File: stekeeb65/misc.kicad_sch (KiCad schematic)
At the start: 7 parts, among them J1 TYPE-C-31-M12_13_EDITED, J2 Conn_02x03_Odd_Even, U1 WE-TVS-82400102

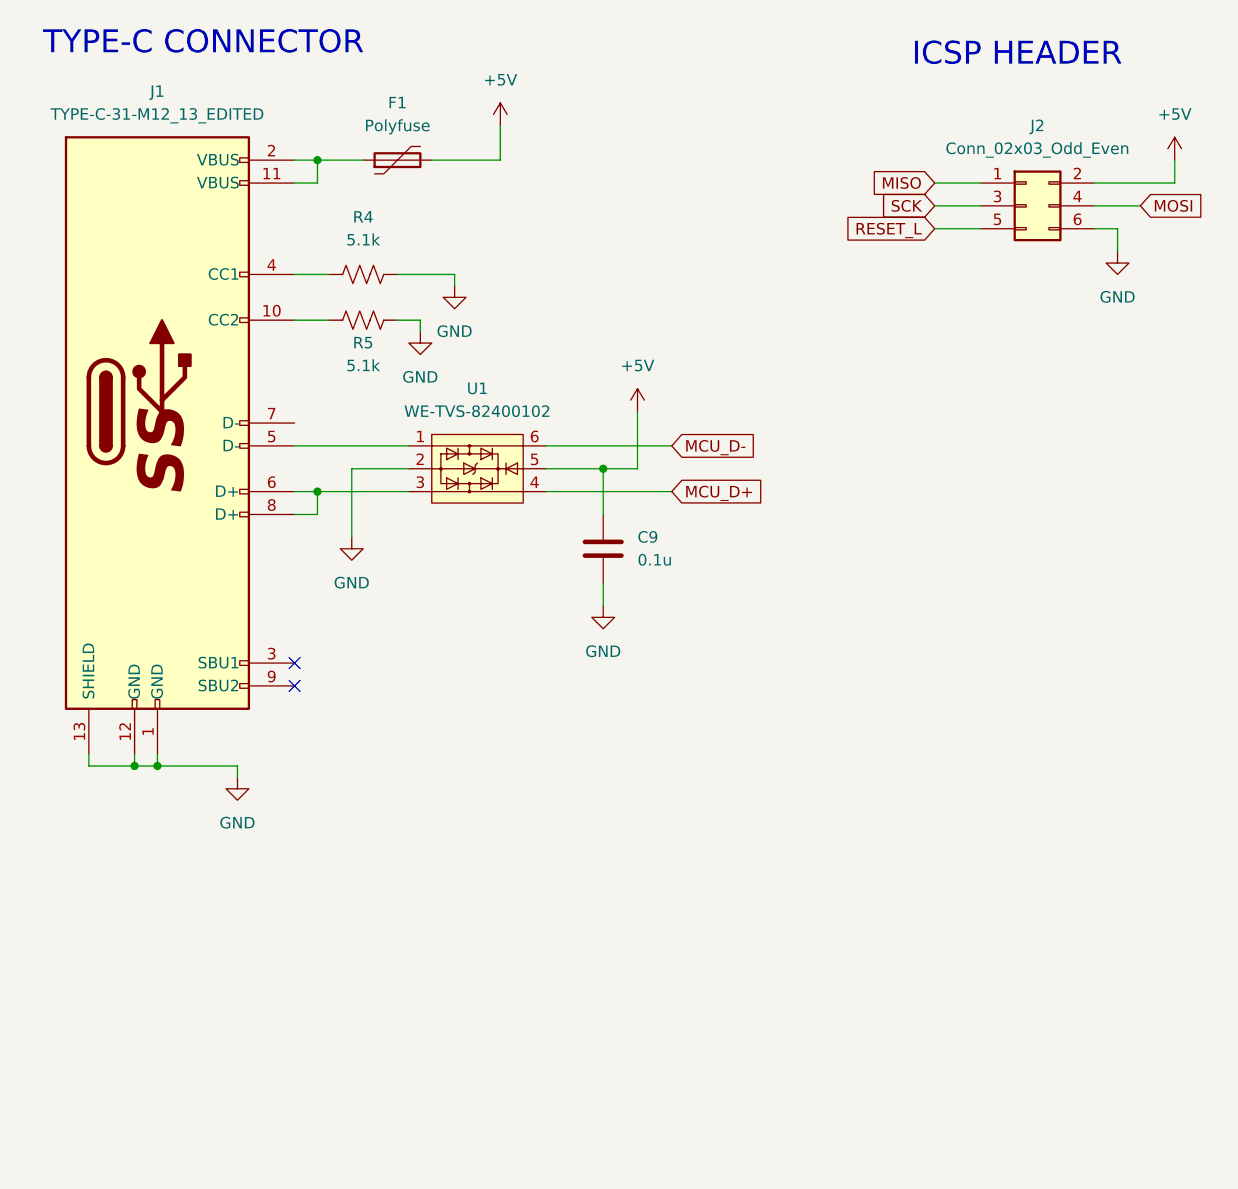
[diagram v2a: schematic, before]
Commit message: Adding key layout with leds
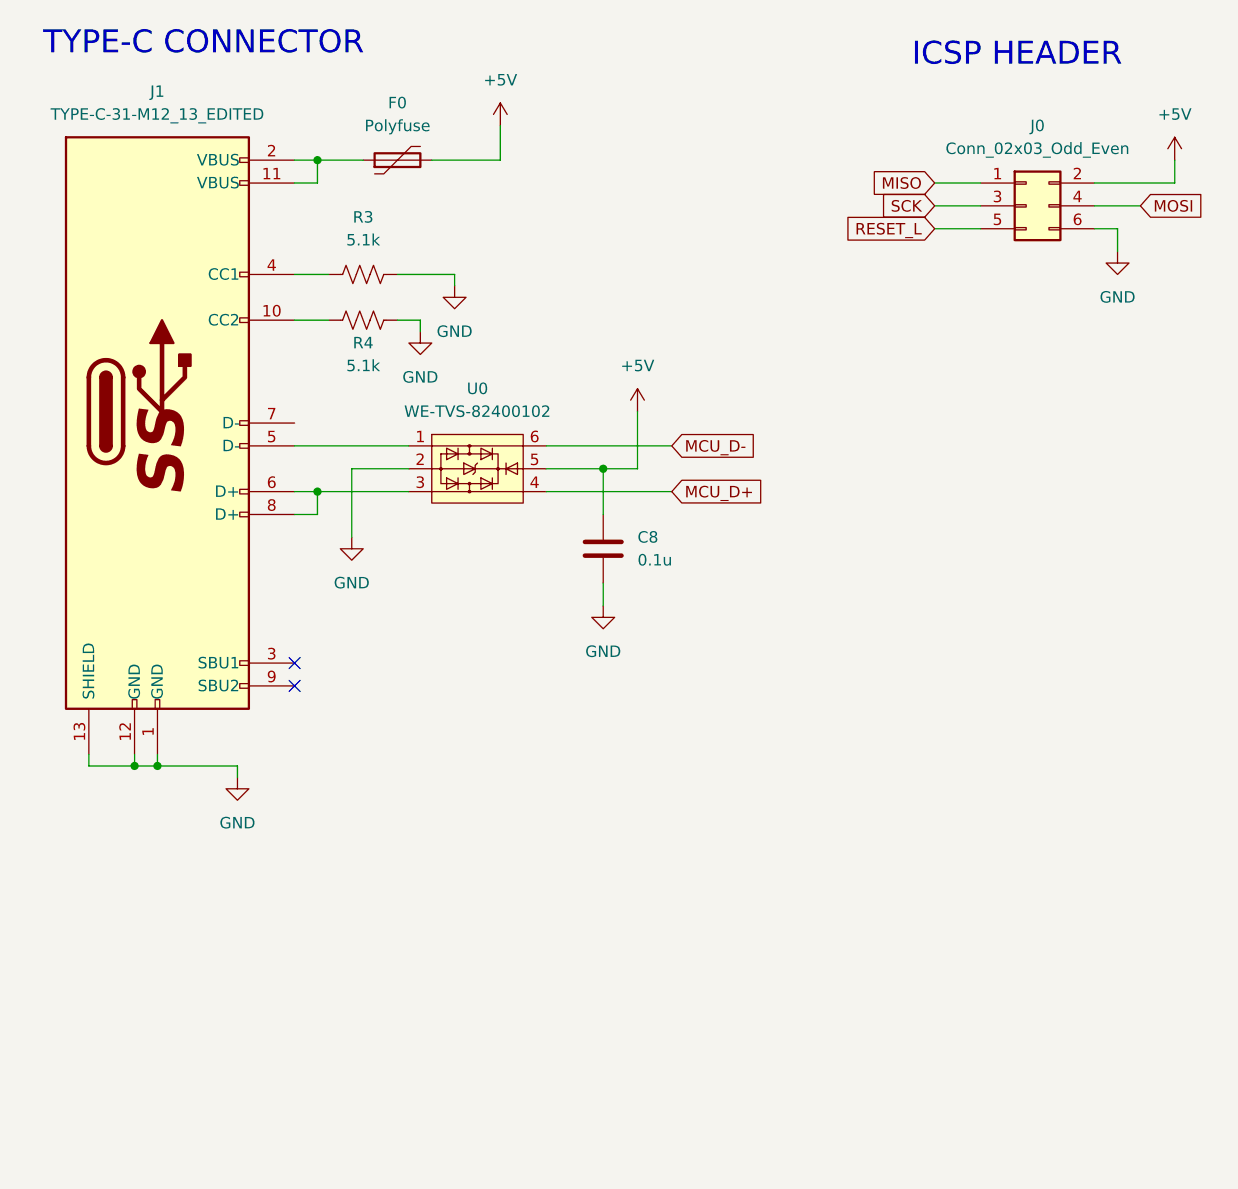
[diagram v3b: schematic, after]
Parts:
- renumbered C9 to C8, F1 to F0, J2 to J0, R4 to R3, R5 to R4, U1 to U0
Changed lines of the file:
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@@
   (symbol (lib_id "power:GND") (at 88.9 83.82 0) (unit 1)
     (in_bom yes) (on_board yes) (fields_autoplaced)
-    (property "Reference" "#PWR020" (id 0) (at 88.9 90.17 0)
+    (property "Reference" "#PWR021" (id 0) (at 88.9 90.17 0)
       (effects (font (size 1.27 1.27)) hide)
     )
@@
   (symbol (lib_id "Device:C") (at 88.9 77.47 0) (unit 1)
     (in_bom yes) (on_board yes) (fields_autoplaced)
-    (property "Reference" "C9" (id 0) (at 92.71 76.1999 0)
+    (property "Reference" "C8" (id 0) (at 92.71 76.1999 0)
       (effects (font (size 1.27 1.27)) (justify left))
     )
@@
   (symbol (lib_id "power:GND") (at 60.96 76.2 0) (unit 1)
     (in_bom yes) (on_board yes) (fields_autoplaced)
-    (property "Reference" "#PWR016" (id 0) (at 60.96 82.55 0)
+    (property "Reference" "#PWR020" (id 0) (at 60.96 82.55 0)
       (effects (font (size 1.27 1.27)) hide)
     )
@@
   (symbol (lib_id "power:GND") (at 72.39 48.26 0) (unit 1)
     (in_bom yes) (on_board yes) (fields_autoplaced)
-    (property "Reference" "#PWR018" (id 0) (at 72.39 54.61 0)
+    (property "Reference" "#PWR017" (id 0) (at 72.39 54.61 0)
       (effects (font (size 1.27 1.27)) hide)
     )
@@
   (symbol (lib_id "Device:R_US") (at 62.23 46.99 90) (unit 1)
     (in_bom yes) (on_board yes) (fields_autoplaced)
-    (property "Reference" "R4" (id 0) (at 62.23 40.64 90))
+    (property "Reference" "R3" (id 0) (at 62.23 40.64 90))
     (property "Value" "5.1k" (id 1) (at 62.23 43.18 90))
     (property "Footprint" "Resistor_SMD:R_0805_2012Metric_Pad1.20x1.40mm_HandSolder" (id 2) (at 62.484 45.974 90)
@@
   (symbol (lib_id "power:+5V") (at 92.71 62.23 0) (unit 1)
     (in_bom yes) (on_board yes) (fields_autoplaced)
-    (property "Reference" "#PWR021" (id 0) (at 92.71 66.04 0)
+    (property "Reference" "#PWR019" (id 0) (at 92.71 66.04 0)
       (effects (font (size 1.27 1.27)) hide)
     )
@@
   (symbol (lib_id "Device:R_US") (at 62.23 52.07 90) (unit 1)
     (in_bom yes) (on_board yes)
-    (property "Reference" "R5" (id 0) (at 62.23 54.61 90))
+    (property "Reference" "R4" (id 0) (at 62.23 54.61 90))
     (property "Value" "5.1k" (id 1) (at 62.23 57.15 90))
     (property "Footprint" "Resistor_SMD:R_0805_2012Metric_Pad1.20x1.40mm_HandSolder" (id 2) (at 62.484 51.054 90)
@@
   (symbol (lib_id "power:GND") (at 146.05 44.45 0) (unit 1)
     (in_bom yes) (on_board yes) (fields_autoplaced)
-    (property "Reference" "#PWR022" (id 0) (at 146.05 50.8 0)
+    (property "Reference" "#PWR016" (id 0) (at 146.05 50.8 0)
       (effects (font (size 1.27 1.27)) hide)
     )
@@
   (symbol (lib_id "power:GND") (at 48.26 102.87 0) (unit 1)
     (in_bom yes) (on_board yes) (fields_autoplaced)
-    (property "Reference" "#PWR015" (id 0) (at 48.26 109.22 0)
+    (property "Reference" "#PWR022" (id 0) (at 48.26 109.22 0)
       (effects (font (size 1.27 1.27)) hide)
     )
@@
   (symbol (lib_id "power:+5V") (at 77.47 30.48 0) (unit 1)
     (in_bom yes) (on_board yes) (fields_autoplaced)
-    (property "Reference" "#PWR019" (id 0) (at 77.47 34.29 0)
+    (property "Reference" "#PWR014" (id 0) (at 77.47 34.29 0)
       (effects (font (size 1.27 1.27)) hide)
     )
@@
   (symbol (lib_id "power:+5V") (at 152.4 34.29 0) (unit 1)
     (in_bom yes) (on_board yes) (fields_autoplaced)
-    (property "Reference" "#PWR023" (id 0) (at 152.4 38.1 0)
+    (property "Reference" "#PWR015" (id 0) (at 152.4 38.1 0)
       (effects (font (size 1.27 1.27)) hide)
     )
@@
   (symbol (lib_id "Power_Protection:WE-TVS-82400102") (at 74.93 68.58 0) (unit 1)
     (in_bom yes) (on_board yes) (fields_autoplaced)
-    (property "Reference" "U1" (id 0) (at 74.93 59.69 0))
+    (property "Reference" "U0" (id 0) (at 74.93 59.69 0))
     (property "Value" "WE-TVS-82400102" (id 1) (at 74.93 62.23 0))
     (property "Footprint" "Package_TO_SOT_SMD:SOT-23-6" (id 2) (at 74.93 73.66 0)
@@
   (symbol (lib_id "power:GND") (at 68.58 53.34 0) (unit 1)
     (in_bom yes) (on_board yes) (fields_autoplaced)
-    (property "Reference" "#PWR017" (id 0) (at 68.58 59.69 0)
+    (property "Reference" "#PWR018" (id 0) (at 68.58 59.69 0)
       (effects (font (size 1.27 1.27)) hide)
     )
@@
   (symbol (lib_id "Connector_Generic:Conn_02x03_Odd_Even") (at 135.89 39.37 0) (unit 1)
     (in_bom yes) (on_board yes) (fields_autoplaced)
-    (property "Reference" "J2" (id 0) (at 137.16 30.48 0))
+    (property "Reference" "J0" (id 0) (at 137.16 30.48 0))
     (property "Value" "Conn_02x03_Odd_Even" (id 1) (at 137.16 33.02 0))
     (property "Footprint" "Connector_PinHeader_2.54mm:PinHeader_2x03_P2.54mm_Vertical" (id 2) (at 135.89 39.37 0)
@@
   (symbol (lib_id "Device:Polyfuse") (at 66.04 34.29 90) (unit 1)
     (in_bom yes) (on_board yes) (fields_autoplaced)
-    (property "Reference" "F1" (id 0) (at 66.04 27.94 90))
+    (property "Reference" "F0" (id 0) (at 66.04 27.94 90))
     (property "Value" "Polyfuse" (id 1) (at 66.04 30.48 90))
     (property "Footprint" "Fuse:Fuse_0805_2012Metric_Pad1.15x1.40mm_HandSolder" (id 2) (at 71.12 33.02 0)
